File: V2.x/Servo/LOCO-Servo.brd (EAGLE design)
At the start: 43.2 x 34.3 mm, 49 parts, among them IC1 Atmega 328-P, IC2 MCP2515, IC3 LM340MP-05, Q1 8MHz, Q2 16MHz, X2 2X6-A

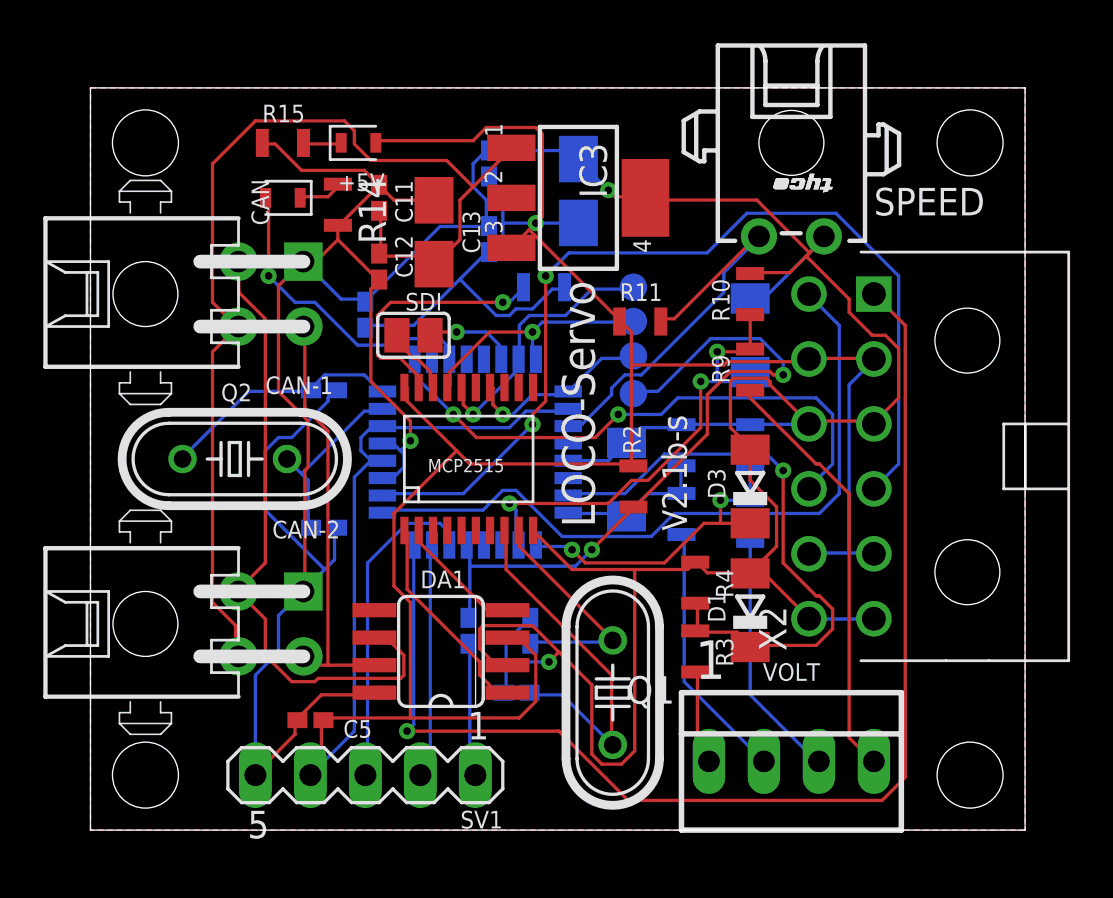
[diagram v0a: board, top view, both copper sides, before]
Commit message: added Loco-CAN icon to motor, servo and switch boards
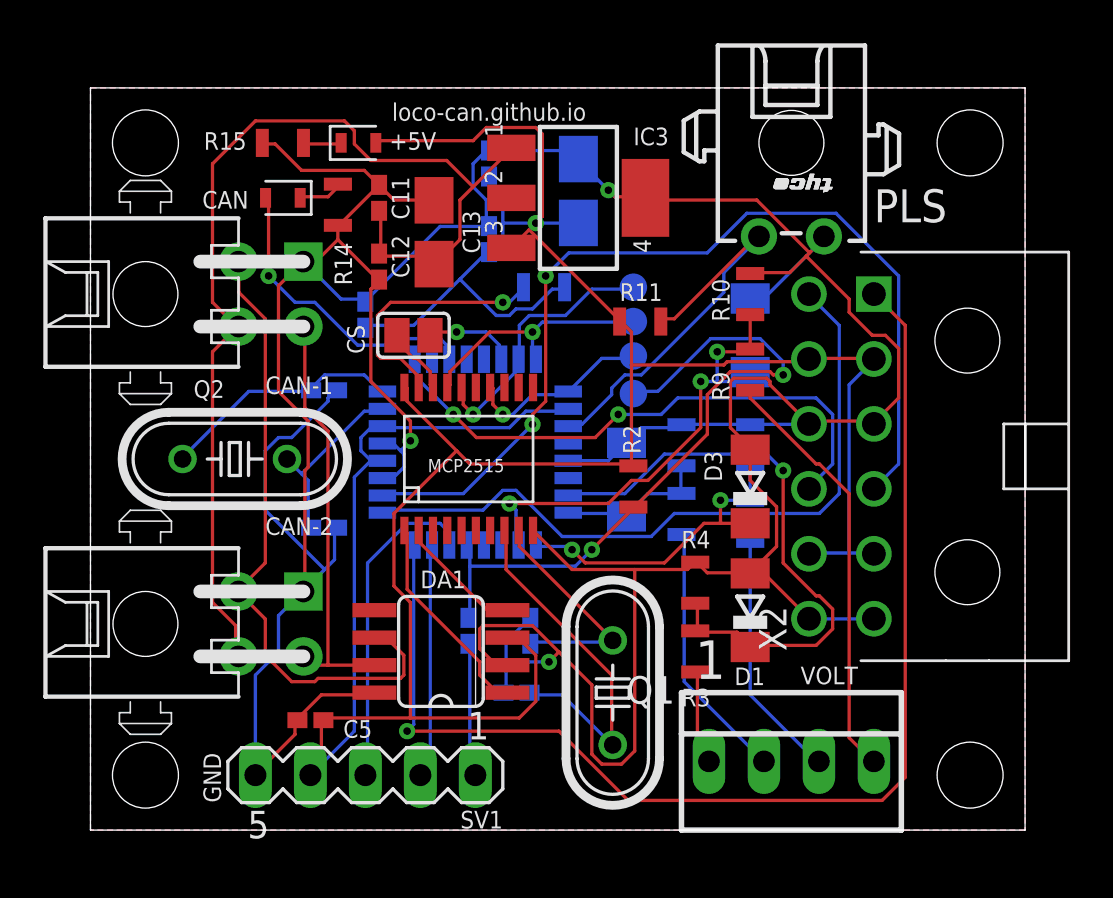
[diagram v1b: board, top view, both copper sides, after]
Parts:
- renumbered SDI to CS, SO1 to RS, SPEED to PLS
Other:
- board text added: "C:/Users/Tom/Nextcloud/Technik/Projekte/Eisenbahn/Gartenbahn/Loco-CAN/Loco-CAN-Hardware/Graphics/Loco-can Logo.bmp"
- board text added: "GND"
- board text added: "Servo"
- board text added: "V2.2"
- board text added: "loco-can.github.io"
- board text removed: "LOCO-Servo"
- board text removed: "V2.1a-s"
- board text removed: "V2.1b-s"
